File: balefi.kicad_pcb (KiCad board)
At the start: 2 copper layers, 2 parts, among them J1 Connectors_EFI_ECUs_Con_82521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, M2 Module:mega-mcu100/0.3

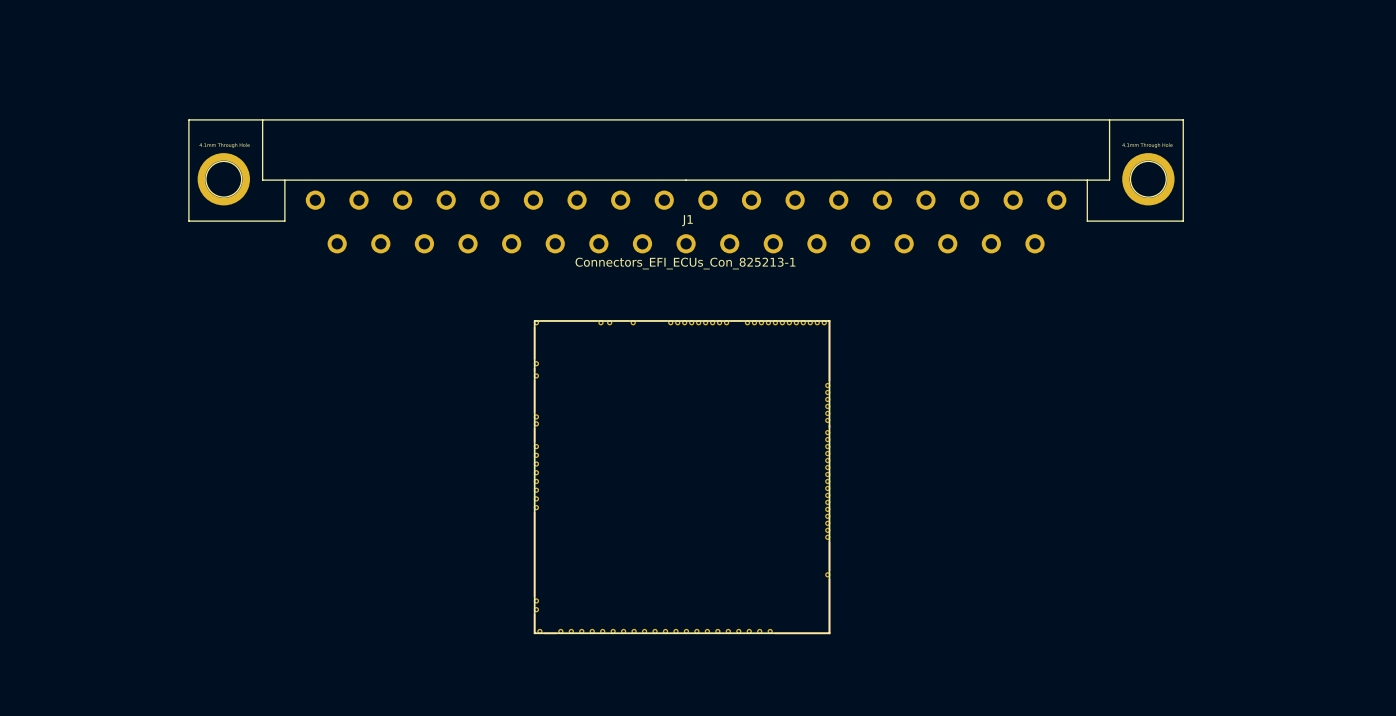
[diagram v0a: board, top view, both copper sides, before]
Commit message: Added outer dimmensions for PCB, added origin point
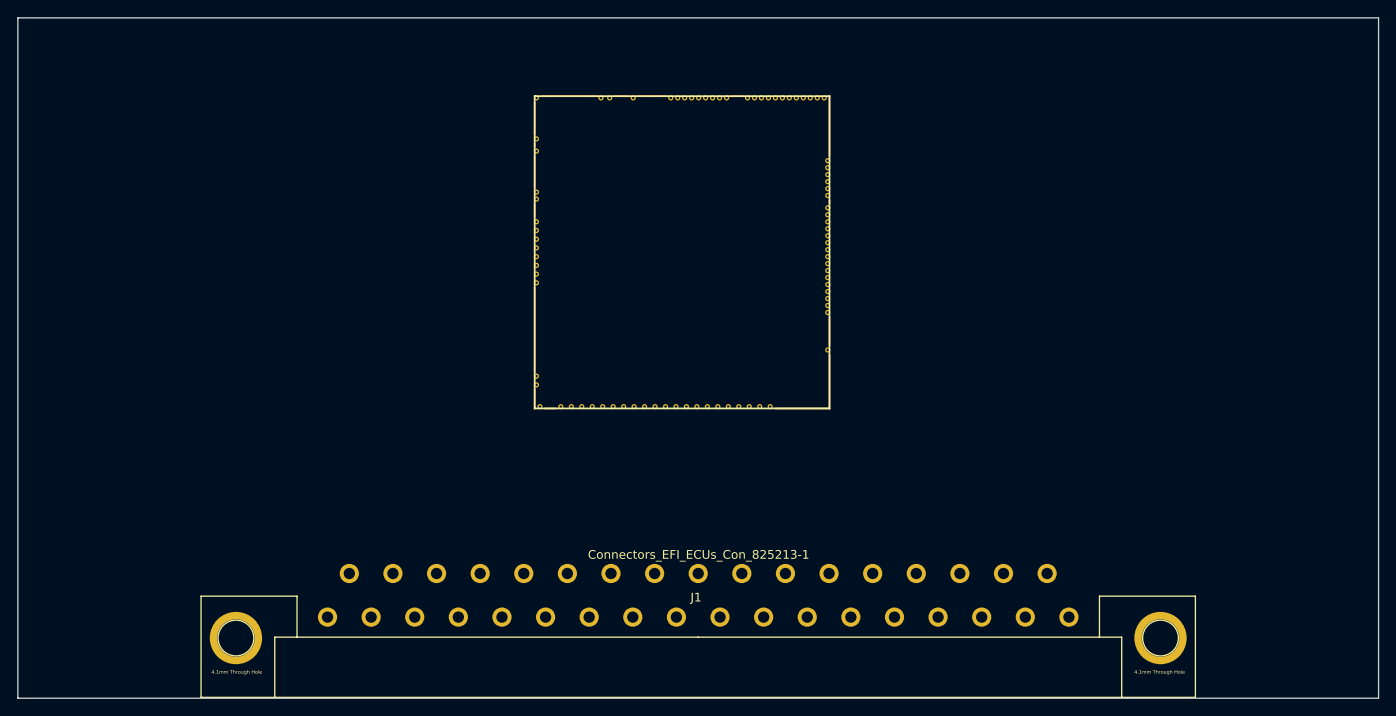
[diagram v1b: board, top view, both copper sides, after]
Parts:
- moved J1 52.4 mm to (150.0, 130.0), turned to 180 degrees
- moved M2 25.8 mm to (131.1, 103.9)
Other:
- board outline added: 156 x 78 mm

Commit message: Started designing schematic
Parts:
- added ?: , , F.Cu at (77.2, 63.4)
- added ?: , , F.Cu at (75.8, 130.0)
- added H1: MountingHole_Pad, MountingHole:MountingHole_3.7mm_Pad_Via, F.Cu at (87.8, 131.0)
- added H2: MountingHole_Pad, MountingHole:MountingHole_3.7mm_Pad_Via, F.Cu at (211.8, 131.0)
- added H3: MountingHole, MountingHole:MountingHole_3.7mm, F.Cu at (156.0, 63.0)
- J1: footprint rusefi_lib:825213-1 -> rusefi_lib:825213-1_FIAT
- moved M2 42.4 mm to (173.3, 99.2)
- moved J1 8.00 mm to (150.0, 138.0)
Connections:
- J1 pad 1: unconnected-(J1-Pad1) -> /IGN14
- J1 pad 10: unconnected-(J1-Pad10) -> /CANL
- J1 pad 11: unconnected-(J1-Pad11) -> /CRANK-
- J1 pad 12: unconnected-(J1-Pad12) -> /AGND
- J1 pad 13: unconnected-(J1-Pad13) -> /CLT
- J1 pad 14: unconnected-(J1-Pad14) -> /5V
- J1 pad 15: unconnected-(J1-Pad15) -> /CANH
- J1 pad 16: unconnected-(J1-Pad16) -> /AGND
- J1 pad 17: unconnected-(J1-Pad17) -> /PGND
- J1 pad 18: unconnected-(J1-Pad18) -> /INJ1
- J1 pad 19: unconnected-(J1-Pad19) -> /IGN23
- J1 pad 2: unconnected-(J1-Pad2) -> /ETB2
- J1 pad 20: unconnected-(J1-Pad20) -> /ETB1
- J1 pad 21: unconnected-(J1-Pad21) -> /INJ3
- J1 pad 22: unconnected-(J1-Pad22) -> /TACHO_OUT
- J1 pad 23: unconnected-(J1-Pad23) -> /FPUMP_RELAY
- J1 pad 24: unconnected-(J1-Pad24) -> /FUEL_PRESS
- J1 pad 25: unconnected-(J1-Pad25) -> /OIL_TEMP
- J1 pad 26: unconnected-(J1-Pad26) -> /IGNITION
- J1 pad 27: unconnected-(J1-Pad27) -> /PPS1_IN
- J1 pad 28: unconnected-(J1-Pad28) -> /CRANK+
- J1 pad 29: unconnected-(J1-Pad29) -> /KNOCK_IN
- J1 pad 3: unconnected-(J1-Pad3) -> /FAN_OUT
- J1 pad 30: unconnected-(J1-Pad30) -> /TPS
- J1 pad 31: unconnected-(J1-Pad31) -> /IAT
- J1 pad 32: unconnected-(J1-Pad32) -> /MAP
- J1 pad 33: unconnected-(J1-Pad33) -> /CAM
- J1 pad 34: unconnected-(J1-Pad34) -> /FLEX_IN
- J1 pad 35: unconnected-(J1-Pad35) -> /INJ2
- J1 pad 4: unconnected-(J1-Pad4) -> /INJ4
- J1 pad 5: unconnected-(J1-Pad5) -> /BOOST_OUT
- J1 pad 6: unconnected-(J1-Pad6) -> /MIL
- J1 pad 7: unconnected-(J1-Pad7) -> /VSS
- J1 pad 8: unconnected-(J1-Pad8) -> /OIL_PRESS
- J1 pad 9: unconnected-(J1-Pad9) -> /PPS2_IN
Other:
- board size 156 x 78 mm -> 146 x 78 mm

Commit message: a lot of changes
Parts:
- removed ? (x2): , 
- removed M2: Module:mega-mcu100/0.3, hellen-one-mega-mcu100-0.3:mega-mcu100
- added C1: 10nF, Capacitor_SMD:C_0402_1005Metric, F.Cu at (58.4, 75.1)
- added C10: 10nF, Capacitor_SMD:C_0402_1005Metric, F.Cu at (119.7, 117.3)
- added C100: 10uF, Capacitor_SMD:C_1206_3216Metric, F.Cu at (86.2, 73.0)
- added C101: 10uF, Capacitor_SMD:C_1206_3216Metric, F.Cu at (86.2, 76.4)
- added C102: 10uF, Capacitor_SMD:C_1206_3216Metric, F.Cu at (86.2, 79.7)
- added C103: 100nF, Capacitor_SMD:C_0402_1005Metric, F.Cu at (90.5, 83.5)
- added C104: 10uF, Capacitor_SMD:C_1206_3216Metric, F.Cu at (86.2, 83.1)
- added C105: 100nF, Capacitor_SMD:C_0402_1005Metric, F.Cu at (90.5, 85.5)
- added C106: 100nF, Capacitor_SMD:C_0402_1005Metric, F.Cu at (167.5, 65.0)
- added C107: 1uF, Capacitor_SMD:C_0805_2012Metric, F.Cu at (147.3, 116.0)
- added C108: 100nF, Capacitor_SMD:C_0402_1005Metric, F.Cu at (145.7, 116.8)
- added C109: 10nF, Capacitor_SMD:C_0402_1005Metric, F.Cu at (142.5, 117.8)
- added C11: 100uF, Capacitor_SMD:CP_Elec_8x10, F.Cu at (212.0, 87.7)
- added C12: 1uF, Capacitor_SMD:C_0805_2012Metric, F.Cu at (212.0, 77.2)
- added C13: 100nF, Capacitor_SMD:C_0402_1005Metric, F.Cu at (212.2, 75.6)
- added C14: 100nF, Capacitor_SMD:C_0402_1005Metric, F.Cu at (210.2, 74.0)
- added C15: 10uF, Capacitor_SMD:C_1206_3216Metric, F.Cu at (206.8, 74.4)
- added C16: 10uF, Capacitor_SMD:C_1206_3216Metric, F.Cu at (206.8, 76.8)
- added C17: 10uF, Capacitor_SMD:C_1206_3216Metric, F.Cu at (206.8, 79.2)
- added C18: 10uF, Capacitor_SMD:C_1206_3216Metric, F.Cu at (202.2, 79.2)
- added C19: 10uF, Capacitor_SMD:C_1206_3216Metric, F.Cu at (202.2, 76.8)
- added C2: 10nF, Capacitor_SMD:C_0402_1005Metric, F.Cu at (58.4, 77.6)
- added C20: 10uF, Capacitor_SMD:C_1206_3216Metric, F.Cu at (202.2, 74.4)
- added C21: 10uF, Capacitor_SMD:C_1206_3216Metric, F.Cu at (212.2, 118.0)
- added C22: 10uF, Capacitor_SMD:C_1206_3216Metric, F.Cu at (214.8, 93.3)
- added C23: 10nF, Capacitor_SMD:C_0402_1005Metric, F.Cu at (214.1, 66.5)
- added C24: 1uF, Capacitor_SMD:C_0805_2012Metric, F.Cu at (177.1, 111.2)
- added C25: 1uF, Capacitor_SMD:C_0805_2012Metric, F.Cu at (186.8, 110.9)
- added C26: 10uF, Capacitor_SMD:C_1206_3216Metric, F.Cu at (194.0, 93.5)
- added C27: 100nF, Capacitor_SMD:C_0402_1005Metric, F.Cu at (49.7, 96.8)
- added C28: 100nF, Capacitor_SMD:C_0402_1005Metric, F.Cu at (195.1, 95.3)
- added C29: 100nF, Capacitor_SMD:C_0402_1005Metric, F.Cu at (195.1, 100.7)
- added C3: 10nF, Capacitor_SMD:C_0402_1005Metric, F.Cu at (58.4, 80.1)
- added C30: 1uF, Capacitor_SMD:C_0805_2012Metric, F.Cu at (194.6, 102.3)
- added C31: 10uF, Capacitor_SMD:C_1206_3216Metric, F.Cu at (194.0, 104.7)
- added C32: 100nF, Capacitor_SMD:C_0402_1005Metric, F.Cu at (79.2, 26.8)
- added C33: 390pF, Capacitor_SMD:C_0402_1005Metric, F.Cu at (71.0, 17.0)
- added C34: 390pF, Capacitor_SMD:C_0402_1005Metric, F.Cu at (71.0, 19.5)
- added C35: 390pF, Capacitor_SMD:C_0402_1005Metric, F.Cu at (71.0, 22.0)
- added C36: 390pF, Capacitor_SMD:C_0402_1005Metric, F.Cu at (71.0, 24.5)
- added C37: 100nF, Capacitor_SMD:C_0402_1005Metric, F.Cu at (98.5, 27.0)
- added C38: 390pF, Capacitor_SMD:C_0402_1005Metric, F.Cu at (90.3, 17.2)
- added C39: 390pF, Capacitor_SMD:C_0402_1005Metric, F.Cu at (90.3, 19.7)
- added C4: 100nF, Capacitor_SMD:C_0402_1005Metric, F.Cu at (58.4, 82.6)
- added C40: 390pF, Capacitor_SMD:C_0402_1005Metric, F.Cu at (90.3, 22.2)
- added C41: 390pF, Capacitor_SMD:C_0402_1005Metric, F.Cu at (90.3, 24.8)
- added C42: 100nF, Capacitor_SMD:C_0402_1005Metric, F.Cu at (93.0, 101.1)
- added C43: 100nF, Capacitor_SMD:C_0402_1005Metric, F.Cu at (93.0, 99.0)
- added C44: 100nF, Capacitor_SMD:C_0402_1005Metric, F.Cu at (124.3, 89.0)
- added C45: 100nF, Capacitor_SMD:C_0402_1005Metric, F.Cu at (138.3, 91.3)
- added C46: 100nF, Capacitor_SMD:C_0402_1005Metric, F.Cu at (133.9, 71.9)
- added C47: 100nF, Capacitor_SMD:C_0402_1005Metric, F.Cu at (122.5, 76.8)
- added C48: 100nF, Capacitor_SMD:C_0402_1005Metric, F.Cu at (141.9, 76.3)
- added C49: 100nF, Capacitor_SMD:C_0402_1005Metric, F.Cu at (129.6, 72.0)
- added C5: 100nF, Capacitor_SMD:C_0402_1005Metric, F.Cu at (106.2, 114.3)
- added C50: 10uF, Capacitor_SMD:C_1206_3216Metric, F.Cu at (120.5, 80.7)
- added C51: 100nF, Capacitor_SMD:C_0402_1005Metric, F.Cu at (136.3, 72.0)
- added C52: 100nF, Capacitor_SMD:C_0402_1005Metric, F.Cu at (128.1, 71.9)
- added C53: 100nF, Capacitor_SMD:C_0402_1005Metric, F.Cu at (146.8, 84.1)
- added C54: 2.2uF, Capacitor_SMD:C_0805_2012Metric, F.Cu at (120.8, 87.5)
- added C55: 2.2uF, Capacitor_SMD:C_0805_2012Metric, F.Cu at (121.1, 83.9)
- added C56: 15pF, Capacitor_SMD:C_0402_1005Metric, F.Cu at (137.0, 67.6)
- added C57: 15pF, Capacitor_SMD:C_0402_1005Metric, F.Cu at (135.6, 67.6)
- added C58: 6pF, Capacitor_SMD:C_0402_1005Metric, F.Cu at (134.0, 67.2)
- added C59: 6pF, Capacitor_SMD:C_0402_1005Metric, F.Cu at (129.3, 67.3)
- added C6: 100uF, Capacitor_SMD:CP_Elec_8x10, F.Cu at (107.7, 106.3)
- added C60: 100nF, Capacitor_SMD:C_0402_1005Metric, F.Cu at (117.8, 26.7)
- added C61: 390pF, Capacitor_SMD:C_0402_1005Metric, F.Cu at (109.6, 16.9)
- added C62: 390pF, Capacitor_SMD:C_0402_1005Metric, F.Cu at (109.6, 19.4)
- added C63: 390pF, Capacitor_SMD:C_0402_1005Metric, F.Cu at (109.6, 22.0)
- added C64: 390pF, Capacitor_SMD:C_0402_1005Metric, F.Cu at (109.6, 24.5)
- added C65: 100nF, Capacitor_SMD:C_0402_1005Metric, F.Cu at (168.9, 101.4)
- added C66: 4.7nF, Capacitor_SMD:C_0402_1005Metric, F.Cu at (168.9, 114.7)
- added C67: 100nF, Capacitor_SMD:C_0402_1005Metric, F.Cu at (165.6, 107.8)
- added C68: 10nF, Capacitor_SMD:C_0402_1005Metric, F.Cu at (73.5, 35.4)
- added C69: 10nF, Capacitor_SMD:C_0402_1005Metric, F.Cu at (73.5, 38.0)
- added C7: 1uF, Capacitor_SMD:C_0805_2012Metric, F.Cu at (103.8, 114.2)
- added C70: 10nF, Capacitor_SMD:C_0402_1005Metric, F.Cu at (73.5, 40.5)
- added C71: 10nF, Capacitor_SMD:C_0402_1005Metric, F.Cu at (73.5, 43.0)
- added C72: 10nF, Capacitor_SMD:C_0402_1005Metric, F.Cu at (111.5, 34.3)
- added C73: 10nF, Capacitor_SMD:C_0402_1005Metric, F.Cu at (111.5, 36.8)
- added C74: 10nF, Capacitor_SMD:C_0402_1005Metric, F.Cu at (111.5, 39.3)
- added C75: 10nF, Capacitor_SMD:C_0402_1005Metric, F.Cu at (111.5, 41.8)
- added C76: 10nF, Capacitor_SMD:C_0402_1005Metric, F.Cu at (92.0, 35.4)
- added C77: 10nF, Capacitor_SMD:C_0402_1005Metric, F.Cu at (92.0, 37.9)
- added C78: 10nF, Capacitor_SMD:C_0402_1005Metric, F.Cu at (92.0, 40.5)
- added C79: 10nF, Capacitor_SMD:C_0402_1005Metric, F.Cu at (92.0, 43.0)
- added C8: 100nF, Capacitor_SMD:C_0402_1005Metric, F.Cu at (104.3, 115.8)
- added C80: 100nF, Capacitor_SMD:C_0402_1005Metric, F.Cu at (157.7, 113.3)
- added C81: 2.2uF, Capacitor_SMD:C_0805_2012Metric, F.Cu at (156.0, 119.3)
- added C82: 2.2uF, Capacitor_SMD:C_0805_2012Metric, F.Cu at (156.0, 117.2)
- added C83: 3.3nF, Capacitor_SMD:C_0402_1005Metric, F.Cu at (161.2, 122.4)
- added C84: 47pF, Capacitor_SMD:C_0402_1005Metric, F.Cu at (160.2, 112.9)
- added C85: 680pF, Capacitor_SMD:C_0402_1005Metric, F.Cu at (162.4, 116.2)
- added C86: 330pF, Capacitor_SMD:C_0402_1005Metric, F.Cu at (159.2, 112.9)
- added C87: 100nF, Capacitor_SMD:C_0402_1005Metric, F.Cu at (139.0, 174.9)
- added C88: 10uF, Capacitor_SMD:C_1206_3216Metric, F.Cu at (156.5, 177.5)
- added C89: 1nF, Capacitor_SMD:C_0805_2012Metric, F.Cu at (144.4, 178.1)
- added C9: 10nF, Capacitor_SMD:C_0402_1005Metric, F.Cu at (106.2, 117.3)
- added C90: 1nF, Capacitor_SMD:C_0805_2012Metric, F.Cu at (147.4, 178.1)
- added C91: 10uF, Capacitor_SMD:C_1206_3216Metric, F.Cu at (190.7, 68.8)
- added C92: 100nF, Capacitor_SMD:C_0402_1005Metric, F.Cu at (190.7, 71.8)
- added C93: 10uF, Capacitor_SMD:C_1206_3216Metric, F.Cu at (86.2, 63.0)
- added C94: 100nF, Capacitor_SMD:C_0402_1005Metric, F.Cu at (90.5, 75.6)
- added C95: 100nF, Capacitor_SMD:C_0402_1005Metric, F.Cu at (90.5, 77.6)
- added C96: 10uF, Capacitor_SMD:C_1206_3216Metric, F.Cu at (86.2, 66.3)
- added C97: 10uF, Capacitor_SMD:C_1206_3216Metric, F.Cu at (86.2, 69.7)
- added C98: 100nF, Capacitor_SMD:C_0402_1005Metric, F.Cu at (90.5, 79.6)
- added C99: 100nF, Capacitor_SMD:C_0402_1005Metric, F.Cu at (90.5, 81.5)
- added D1: NSVRB751V40T1G, Diode_SMD:D_SOD-323, F.Cu at (70.5, 75.3)
- added D10: V3P6HM3_A/H, Diode_SMD:Vishay_SMPA, F.Cu at (209.1, 69.9)
- added D11: LED, LED_SMD:LED_0603_1608Metric, F.Cu at (175.1, 111.0)
- added D12: 1N4148WS, Diode_SMD:D_SOD-323, F.Cu at (195.3, 90.7)
- added D13: 1N4148WS, Diode_SMD:D_SOD-323, F.Cu at (193.3, 90.7)
- added D14: 1N4148WS, Diode_SMD:D_SOD-323, F.Cu at (138.4, 72.2)
- added D15: LED, LED_SMD:LED_0603_1608Metric, F.Cu at (91.3, 103.8)
- added D16: LED, LED_SMD:LED_0603_1608Metric, F.Cu at (100.2, 103.6)
- added D17: LED, LED_SMD:LED_0603_1608Metric, F.Cu at (122.4, 63.8)
- added D18: LED, LED_SMD:LED_0603_1608Metric, F.Cu at (122.4, 66.3)
- added D19: LED, LED_SMD:LED_0603_1608Metric, F.Cu at (122.4, 68.9)
- added D2: NSVRB751V40T1G, Diode_SMD:D_SOD-323, F.Cu at (70.5, 78.2)
- added D20: LED, LED_SMD:LED_0603_1608Metric, F.Cu at (122.4, 71.5)
- added D21: SZNUP2105L, Package_TO_SOT_SMD:SOT-23, F.Cu at (168.8, 117.8)
- added D22: NUP4202W1T2G, Package_TO_SOT_SMD:SOT-363_SC-70-6, F.Cu at (77.6, 52.0)
- added D23: NUP4202W1T2G, Package_TO_SOT_SMD:SOT-363_SC-70-6, F.Cu at (115.7, 50.9)
- added D24: NUP4202W1T2G, Package_TO_SOT_SMD:SOT-363_SC-70-6, F.Cu at (96.1, 52.0)
- added D25: LED, LED_SMD:LED_0603_1608Metric, F.Cu at (134.2, 174.3)
- added D26: LED, LED_SMD:LED_0603_1608Metric, F.Cu at (136.8, 174.3)
- added D27: 1N4148WS, Diode_SMD:D_SOD-323, F.Cu at (147.0, 76.5)
- added D28: LED, LED_SMD:LED_0603_1608Metric, F.Cu at (103.1, 70.7)
- added D29: V3P6HM3_A/H, Diode_SMD:Vishay_SMPA, F.Cu at (97.5, 71.4)
- added D3: NSVRB751V40T1G, Diode_SMD:D_SOD-323, F.Cu at (70.5, 81.2)
- added D30: PRTR5V0U2X, Package_TO_SOT_SMD:SOT-143, F.Cu at (191.0, 25.0)
- added D31: SZNUP2105L, Package_TO_SOT_SMD:SOT-23, F.Cu at (142.5, 121.5)
- added D4: NSVRB751V40T1G, Diode_SMD:D_SOD-323, F.Cu at (70.5, 84.1)
- added D5: MMSZ4688-TP, Diode_SMD:D_SOD-123, F.Cu at (59.3, 93.0)
- added D6: MMSZ4688-TP, Diode_SMD:D_SOD-123, F.Cu at (59.3, 96.4)
- added D7: V3P6HM3_A/H, Diode_SMD:Vishay_SMPA, F.Cu at (207.2, 116.5)
- added D8: LED, LED_SMD:LED_0603_1608Metric, F.Cu at (214.3, 117.2)
- added D9: LED, LED_SMD:LED_0603_1608Metric, F.Cu at (192.3, 76.9)
- added F1: 350 mA, Fuse:Fuse_1206_3216Metric, F.Cu at (53.5, 75.5)
- added F2: 350 mA, Fuse:Fuse_1206_3216Metric, F.Cu at (53.5, 78.7)
- added F3: 350 mA, Fuse:Fuse_1206_3216Metric, F.Cu at (53.5, 82.0)
- added F4: 350 mA, Fuse:Fuse_1206_3216Metric, F.Cu at (53.5, 85.3)
- added F5: 350 mA, Fuse:Fuse_1206_3216Metric, F.Cu at (53.5, 88.6)
- added F6: 350 mA, Fuse:Fuse_1206_3216Metric, F.Cu at (102.8, 76.3)
- added F7: 350 mA, Fuse:Fuse_1206_3216Metric, F.Cu at (102.8, 79.6)
- added FB1: 600 ohm 500mA, Resistor_SMD:R_0603_1608Metric, F.Cu at (102.0, 82.5)
- added J2: Conn_01x06_Pin, Connector_PinHeader_2.54mm:PinHeader_1x06_P2.54mm_Vertical, F.Cu at (113.0, 98.1)
- added J3: Conn_01x03_Pin, Connector_PinHeader_2.54mm:PinHeader_1x03_P2.54mm_Vertical, F.Cu at (118.0, 98.0)
- added J4: MEM2067-02-180-00-A, footprints:MEM2067-02-180-00-A, F.Cu at (179.2, 69.2)
- added J5: Conn_01x06_Pin, Connector_JST:JST_PH_B6B-PH-K_1x06_P2.00mm_Vertical, F.Cu at (187.8, 18.9)
- added L1: 3,3uH, Inductor_SMD:L_TDK_VLS6045EX_VLS6045AF, F.Cu at (204.1, 69.9)
- added L2: 3,3uH, Inductor_SMD:L_TDK_VLS6045EX_VLS6045AF, F.Cu at (214.3, 98.3)
- added L3: BLM18SP102SN1D, Inductor_SMD:L_0603_1608Metric_Pad1.05x0.95mm_HandSolder, F.Cu at (145.1, 121.7)
- added L4: BLM18SP102SN1D, Inductor_SMD:L_0603_1608Metric_Pad1.05x0.95mm_HandSolder, F.Cu at (139.9, 121.7)
- added NT1: NetTie_2, NetTie:NetTie-2_SMD_Pad2.0mm, F.Cu at (185.0, 119.0)
- added Q1: VND14NV04TR-E, Package_TO_SOT_SMD:TO-252-2, F.Cu at (33.9, 173.7)
- added Q10: PJA3460, Package_TO_SOT_SMD:SOT-23-3, F.Cu at (48.2, 89.4)
- added Q11: PJA3460, Package_TO_SOT_SMD:SOT-23-3, F.Cu at (48.2, 93.8)
- added Q12: DMG2307LQ-7, Package_TO_SOT_SMD:SOT-23-3, F.Cu at (94.5, 76.9)
- added Q13: RUC002N05HZGT116, Package_TO_SOT_SMD:SOT-23, F.Cu at (91.5, 63.5)
- added Q14: DMG2307LQ-7, Package_TO_SOT_SMD:SOT-23-3, F.Cu at (94.5, 81.3)
- added Q15: RUC002N05HZGT116, Package_TO_SOT_SMD:SOT-23, F.Cu at (91.5, 68.0)
- added Q2: VND14NV04TR-E, Package_TO_SOT_SMD:TO-252-2, F.Cu at (62.5, 174.0)
- added Q3: VND14NV04TR-E, Package_TO_SOT_SMD:TO-252-2, F.Cu at (49.4, 174.2)
- added Q4: VND14NV04TR-E, Package_TO_SOT_SMD:TO-252-2, F.Cu at (33.7, 157.5)
- added Q5: RGPR30BM40HRTL, Package_TO_SOT_SMD:TO-252-2, F.Cu at (86.8, 110.0)
- added Q6: RGPR30BM40HRTL, Package_TO_SOT_SMD:TO-252-2, F.Cu at (95.8, 110.0)
- added Q7: PJA3460, Package_TO_SOT_SMD:SOT-23-3, F.Cu at (48.2, 76.0)
- added Q8: PJA3460, Package_TO_SOT_SMD:SOT-23-3, F.Cu at (48.2, 80.5)
- added Q9: PJA3460, Package_TO_SOT_SMD:SOT-23-3, F.Cu at (48.2, 84.9)
- added R1: 330, Resistor_SMD:R_0402_1005Metric, F.Cu at (29.0, 179.0)
- added R10: 1k, Resistor_SMD:R_0402_1005Metric, F.Cu at (98.0, 102.3)
- added R100: 680k, Resistor_SMD:R_0402_1005Metric, F.Cu at (115.0, 42.0)
- added R101: 680k, Resistor_SMD:R_0402_1005Metric, F.Cu at (115.0, 44.0)
- added R102: 680k, Resistor_SMD:R_0402_1005Metric, F.Cu at (115.0, 46.0)
- added R103: 680k, Resistor_SMD:R_0402_1005Metric, F.Cu at (115.0, 48.0)
- added R104: 680k, Resistor_SMD:R_0402_1005Metric, F.Cu at (95.5, 35.2)
- added R105: 680k, Resistor_SMD:R_0402_1005Metric, F.Cu at (95.5, 37.2)
- added R106: 680k, Resistor_SMD:R_0402_1005Metric, F.Cu at (95.5, 39.1)
- added R107: 680k, Resistor_SMD:R_0402_1005Metric, F.Cu at (95.5, 41.1)
- added R108: 4k7, Resistor_SMD:R_0402_1005Metric, F.Cu at (92.0, 45.5)
- added R109: 4k7, Resistor_SMD:R_0402_1005Metric, F.Cu at (92.0, 48.0)
- added R11: 10k, Resistor_SMD:R_1206_3216Metric, F.Cu at (53.5, 91.9)
- added R110: 4k7, Resistor_SMD:R_0402_1005Metric, F.Cu at (92.0, 50.5)
- added R111: 4k7, Resistor_SMD:R_0402_1005Metric, F.Cu at (92.0, 53.0)
- added R112: 680k, Resistor_SMD:R_0402_1005Metric, F.Cu at (95.5, 43.1)
- added R113: 680k, Resistor_SMD:R_0402_1005Metric, F.Cu at (95.5, 45.1)
- added R114: 680k, Resistor_SMD:R_0402_1005Metric, F.Cu at (95.5, 47.1)
- added R115: 680k, Resistor_SMD:R_0402_1005Metric, F.Cu at (95.5, 49.1)
- added R116: 330, Resistor_SMD:R_0402_1005Metric, F.Cu at (157.2, 115.2)
- added R117: 330, Resistor_SMD:R_0402_1005Metric, F.Cu at (156.1, 115.2)
- added R118: 12k, Resistor_SMD:R_0402_1005Metric, F.Cu at (161.9, 117.8)
- added R119: 100k, Resistor_SMD:R_0402_1005Metric, F.Cu at (162.2, 114.6)
- added R12: 330, Resistor_SMD:R_0402_1005Metric, F.Cu at (58.4, 85.1)
- added R120: 33k, Resistor_SMD:R_0402_1005Metric, F.Cu at (161.7, 113.0)
- added R121: 100k, Resistor_SMD:R_0402_1005Metric, F.Cu at (160.2, 121.4)
- added R122: 470k, Resistor_SMD:R_0402_1005Metric, F.Cu at (158.7, 121.0)
- added R123: 10k, Resistor_SMD:R_1206_3216Metric, F.Cu at (110.6, 181.6)
- added R124: 10k, Resistor_SMD:R_1206_3216Metric, F.Cu at (113.8, 181.6)
- added R125: 10k, Resistor_SMD:R_1206_3216Metric, F.Cu at (126.0, 166.8)
- added R126: 10k, Resistor_SMD:R_1206_3216Metric, F.Cu at (126.0, 169.2)
- added R127: 10k, Resistor_SMD:R_0402_1005Metric, F.Cu at (134.1, 178.3)
- added R128: 10k, Resistor_SMD:R_0402_1005Metric, F.Cu at (136.6, 178.3)
- added R129: 10k, Resistor_SMD:R_0402_1005Metric, F.Cu at (139.1, 178.3)
- added R13: 330, Resistor_SMD:R_0402_1005Metric, F.Cu at (58.4, 87.6)
- added R130: 10k, Resistor_SMD:R_0402_1005Metric, F.Cu at (141.7, 178.3)
- added R131: 5k1, Resistor_SMD:R_0603_1608Metric, F.Cu at (150.4, 178.1)
- added R132: 10k, Resistor_SMD:R_1206_3216Metric, F.Cu at (141.0, 183.1)
- added R133: 10k, Resistor_SMD:R_1206_3216Metric, F.Cu at (144.3, 183.1)
- added R134: 10k, Resistor_SMD:R_1206_3216Metric, F.Cu at (147.6, 183.1)
- added R135: 10k, Resistor_SMD:R_1206_3216Metric, F.Cu at (150.8, 183.1)
- added R136: 5k1, Resistor_SMD:R_0603_1608Metric, F.Cu at (153.3, 178.1)
- added R137: 10k, Resistor_SMD:R_1206_3216Metric, F.Cu at (154.1, 183.1)
- added R138: 10k, Resistor_SMD:R_1206_3216Metric, F.Cu at (157.4, 183.1)
- added R139: 4k7, Resistor_SMD:R_0402_1005Metric, F.Cu at (146.8, 79.2)
- added R14: 330, Resistor_SMD:R_0402_1005Metric, F.Cu at (58.4, 90.1)
- added R140: 10k, Resistor_SMD:R_0402_1005Metric, F.Cu at (190.5, 73.7)
- added R141: 1R, Resistor_SMD:R_0603_1608Metric, F.Cu at (192.9, 69.3)
- added R142: 10k, Resistor_SMD:R_0402_1005Metric, F.Cu at (102.0, 85.0)
- added R143: 10k, Resistor_SMD:R_0402_1005Metric, F.Cu at (98.5, 75.7)
- added R144: 10k, Resistor_SMD:R_0402_1005Metric, F.Cu at (98.5, 77.6)
- added R145: 10k, Resistor_SMD:R_0402_1005Metric, F.Cu at (98.5, 79.6)
- added R146: 10k, Resistor_SMD:R_0402_1005Metric, F.Cu at (98.5, 81.6)
- added R147: 5k1, Resistor_SMD:R_0603_1608Metric, F.Cu at (186.9, 24.0)
- added R148: 5k1, Resistor_SMD:R_0603_1608Metric, F.Cu at (186.9, 26.5)
- added R149: 22, Resistor_SMD:R_0402_1005Metric, F.Cu at (143.2, 80.5)
- added R15: 330, Resistor_SMD:R_0402_1005Metric, F.Cu at (62.4, 75.1)
- added R150: 22, Resistor_SMD:R_0402_1005Metric, F.Cu at (143.2, 81.9)
- added R151: 22, Resistor_SMD:R_0402_1005Metric, F.Cu at (143.2, 79.5)
- added R152: 22, Resistor_SMD:R_0402_1005Metric, F.Cu at (171.8, 66.5)
- added R153: 22, Resistor_SMD:R_0402_1005Metric, F.Cu at (141.8, 108.5)
- added R154: 22, Resistor_SMD:R_0402_1005Metric, F.Cu at (142.8, 88.3)
- added R155: 22, Resistor_SMD:R_0402_1005Metric, F.Cu at (142.9, 91.5)
- added R16: 68k, Resistor_SMD:R_0402_1005Metric, F.Cu at (62.4, 77.6)
- added R17: 68k, Resistor_SMD:R_0402_1005Metric, F.Cu at (62.4, 80.1)
- added R18: 68k, Resistor_SMD:R_0402_1005Metric, F.Cu at (62.4, 82.6)
- added R19: 68k, Resistor_SMD:R_0402_1005Metric, F.Cu at (62.4, 85.1)
- added R2: 68k, Resistor_SMD:R_0402_1005Metric, F.Cu at (29.0, 181.5)
- added R20: 33k, Resistor_SMD:R_0402_1005Metric, F.Cu at (62.4, 87.6)
- added R21: 33k, Resistor_SMD:R_0402_1005Metric, F.Cu at (62.4, 90.1)
- added R22: 33k, Resistor_SMD:R_0402_1005Metric, F.Cu at (66.4, 75.1)
- added R23: 330, Resistor_SMD:R_0402_1005Metric, F.Cu at (66.4, 77.6)
- added R24: 100k, Resistor_SMD:R_0402_1005Metric, F.Cu at (66.4, 80.1)
- added R25: 68k, Resistor_SMD:R_0402_1005Metric, F.Cu at (66.4, 82.6)
- added R26: 4k7, Resistor_SMD:R_0402_1005Metric, F.Cu at (121.8, 113.3)
- added R27: 33k, Resistor_SMD:R_0402_1005Metric, F.Cu at (214.6, 119.8)
- added R28: 68k, Resistor_SMD:R_0402_1005Metric, F.Cu at (206.2, 81.0)
- added R29: 10k, Resistor_SMD:R_0402_1005Metric, F.Cu at (216.6, 72.8)
- added R3: 330, Resistor_SMD:R_0402_1005Metric, F.Cu at (57.6, 179.3)
- added R30: 10k, Resistor_SMD:R_0402_1005Metric, F.Cu at (192.4, 79.5)
- added R31: 12k, Resistor_SMD:R_0402_1005Metric, F.Cu at (208.2, 81.0)
- added R32: 1R, Resistor_SMD:R_0603_1608Metric, F.Cu at (211.8, 121.2)
- added R33: 10k, Resistor_SMD:R_0402_1005Metric, F.Cu at (174.8, 113.2)
- added R34: 10k, Resistor_SMD:R_0402_1005Metric, F.Cu at (181.9, 115.2)
- added R35: 1k, Resistor_SMD:R_0402_1005Metric, F.Cu at (46.8, 97.0)
- added R36: 2k7, Resistor_SMD:R_0402_1005Metric, F.Cu at (75.0, 17.0)
- added R37: 2k7, Resistor_SMD:R_0402_1005Metric, F.Cu at (75.0, 19.5)
- added R38: 2k7, Resistor_SMD:R_0402_1005Metric, F.Cu at (75.0, 22.0)
- added R39: 2k7, Resistor_SMD:R_0402_1005Metric, F.Cu at (75.0, 24.5)
- added R4: 68k, Resistor_SMD:R_0402_1005Metric, F.Cu at (57.6, 181.8)
- added R40: 2k7, Resistor_SMD:R_0402_1005Metric, F.Cu at (79.0, 17.0)
- added R41: 2k7, Resistor_SMD:R_0402_1005Metric, F.Cu at (79.0, 19.5)
- added R42: 2k7, Resistor_SMD:R_0402_1005Metric, F.Cu at (79.0, 22.0)
- added R43: 2k7, Resistor_SMD:R_0402_1005Metric, F.Cu at (79.0, 24.5)
- added R44: 2k7, Resistor_SMD:R_0402_1005Metric, F.Cu at (94.3, 17.2)
- added R45: 2k7, Resistor_SMD:R_0402_1005Metric, F.Cu at (94.3, 19.7)
- added R46: 2k7, Resistor_SMD:R_0402_1005Metric, F.Cu at (94.3, 22.2)
- added R47: 2k7, Resistor_SMD:R_0402_1005Metric, F.Cu at (94.3, 24.8)
- added R48: 2k7, Resistor_SMD:R_0402_1005Metric, F.Cu at (98.3, 17.2)
- added R49: 2k7, Resistor_SMD:R_0402_1005Metric, F.Cu at (98.3, 19.7)
- added R5: 330, Resistor_SMD:R_0402_1005Metric, F.Cu at (44.5, 179.5)
- added R50: 2k7, Resistor_SMD:R_0402_1005Metric, F.Cu at (98.3, 22.2)
- added R51: 2k7, Resistor_SMD:R_0402_1005Metric, F.Cu at (98.3, 24.8)
- added R52: 10, Resistor_SMD:R_0402_1005Metric, F.Cu at (93.8, 102.9)
- added R53: 10, Resistor_SMD:R_0402_1005Metric, F.Cu at (95.8, 102.9)
- added R54: 10k, Resistor_SMD:R_0402_1005Metric, F.Cu at (96.0, 96.7)
- added R55: 10k, Resistor_SMD:R_0402_1005Metric, F.Cu at (93.9, 96.7)
- added R56: 1k, Resistor_SMD:R_0402_1005Metric, F.Cu at (91.2, 106.3)
- added R57: 1k, Resistor_SMD:R_0402_1005Metric, F.Cu at (100.2, 106.2)
- added R58: 10k, Resistor_SMD:R_0402_1005Metric, F.Cu at (121.8, 99.4)
- added R59: 10k, Resistor_SMD:R_0402_1005Metric, F.Cu at (121.8, 97.4)
- added R6: 68k, Resistor_SMD:R_0402_1005Metric, F.Cu at (44.5, 182.0)
- added R60: 100, Resistor_SMD:R_0402_1005Metric, F.Cu at (121.8, 95.4)
- added R61: 10, Resistor_SMD:R_0402_1005Metric, F.Cu at (121.8, 93.4)
- added R62: 10, Resistor_SMD:R_0402_1005Metric, F.Cu at (121.8, 91.4)
- added R63: 1k, Resistor_SMD:R_0402_1005Metric, F.Cu at (126.4, 63.7)
- added R64: 0R, Resistor_SMD:R_0402_1005Metric, F.Cu at (121.8, 89.4)
- added R65: 1k, Resistor_SMD:R_0402_1005Metric, F.Cu at (126.4, 66.2)
- added R66: 1k, Resistor_SMD:R_0402_1005Metric, F.Cu at (126.4, 68.7)
- added R67: 1k, Resistor_SMD:R_0402_1005Metric, F.Cu at (126.4, 71.2)
- added R68: 2k7, Resistor_SMD:R_0402_1005Metric, F.Cu at (113.6, 16.9)
- added R69: 2k7, Resistor_SMD:R_0402_1005Metric, F.Cu at (113.6, 19.4)
- added R7: 330, Resistor_SMD:R_0402_1005Metric, F.Cu at (28.8, 162.8)
- added R70: 2k7, Resistor_SMD:R_0402_1005Metric, F.Cu at (113.6, 22.0)
- added R71: 2k7, Resistor_SMD:R_0402_1005Metric, F.Cu at (113.6, 24.5)
- added R72: 2k7, Resistor_SMD:R_0402_1005Metric, F.Cu at (117.7, 16.9)
- added R73: 2k7, Resistor_SMD:R_0402_1005Metric, F.Cu at (117.7, 19.4)
- added R74: 2k7, Resistor_SMD:R_0402_1005Metric, F.Cu at (117.7, 22.0)
- added R75: 2k7, Resistor_SMD:R_0402_1005Metric, F.Cu at (117.7, 24.5)
- added R76: 10, Resistor_SMD:R_0402_1005Metric, F.Cu at (169.5, 110.5)
- added R77: 60.4, Resistor_SMD:R_0805_2012Metric, F.Cu at (170.7, 112.7)
- added R78: 60.4, Resistor_SMD:R_0805_2012Metric, F.Cu at (167.1, 112.7)
- added R79: 10, Resistor_SMD:R_0402_1005Metric, F.Cu at (168.3, 110.5)
- added R8: 68k, Resistor_SMD:R_0402_1005Metric, F.Cu at (28.8, 165.3)
- added R80: 680k, Resistor_SMD:R_0402_1005Metric, F.Cu at (77.0, 35.2)
- added R81: 680k, Resistor_SMD:R_0402_1005Metric, F.Cu at (77.0, 37.2)
- added R82: 680k, Resistor_SMD:R_0402_1005Metric, F.Cu at (77.0, 39.2)
- added R83: 680k, Resistor_SMD:R_0402_1005Metric, F.Cu at (77.0, 41.1)
- added R84: 4k7, Resistor_SMD:R_0402_1005Metric, F.Cu at (73.5, 45.5)
- added R85: 4k7, Resistor_SMD:R_0402_1005Metric, F.Cu at (73.5, 48.0)
- added R86: 4k7, Resistor_SMD:R_0402_1005Metric, F.Cu at (73.5, 50.5)
- added R87: 4k7, Resistor_SMD:R_0402_1005Metric, F.Cu at (73.5, 53.0)
- added R88: 680k, Resistor_SMD:R_0402_1005Metric, F.Cu at (77.0, 43.1)
- added R89: 680k, Resistor_SMD:R_0402_1005Metric, F.Cu at (77.0, 45.1)
- added R9: 1k, Resistor_SMD:R_0402_1005Metric, F.Cu at (89.4, 103.0)
- added R90: 680k, Resistor_SMD:R_0402_1005Metric, F.Cu at (77.0, 47.1)
- added R91: 680k, Resistor_SMD:R_0402_1005Metric, F.Cu at (77.0, 49.1)
- added R92: 680k, Resistor_SMD:R_0402_1005Metric, F.Cu at (115.0, 34.0)
- added R93: 680k, Resistor_SMD:R_0402_1005Metric, F.Cu at (115.0, 36.0)
- added R94: 680k, Resistor_SMD:R_0402_1005Metric, F.Cu at (115.0, 38.0)
- added R95: 680k, Resistor_SMD:R_0402_1005Metric, F.Cu at (115.0, 40.0)
- added R96: 4k7, Resistor_SMD:R_0402_1005Metric, F.Cu at (111.5, 44.3)
- added R97: 4k7, Resistor_SMD:R_0402_1005Metric, F.Cu at (111.5, 46.9)
- added R98: 4k7, Resistor_SMD:R_0402_1005Metric, F.Cu at (111.5, 49.4)
- added R99: 4k7, Resistor_SMD:R_0402_1005Metric, F.Cu at (111.5, 51.9)
- added U1: TLE9201SG, footprints:Infineon_PG-DSO-12-17_ThermalVias, F.Cu at (113.0, 115.3)
- added U10: TJA1051T/3/2Z, Package_SO:SOIC-8_3.9x4.9mm_P1.27mm, F.Cu at (168.9, 105.8)
- added U11: MCP6282T-E/MS, Package_SO:MSOP-8_3x3mm_P0.65mm, F.Cu at (159.6, 117.2)
- added U12: MAX9926, Package_SO:QSOP-16_3.9x4.9mm_P0.635mm, F.Cu at (129.5, 176.1)
- added U13: REF3033, Package_TO_SOT_SMD:SOT-23, F.Cu at (91.5, 72.4)
- added U14: NCV1117DT33T5G, Package_TO_SOT_SMD:TO-252-2, F.Cu at (100.9, 65.3)
- added U15: LPS25HB, Package_LGA:ST_HLGA-10_2.5x2.5mm_P0.6mm_LayoutBorder3x2y, F.Cu at (168.1, 62.0)
- added U16: MAX31855KASA, Package_SO:SOIC-8_3.9x4.9mm_P1.27mm, F.Cu at (142.4, 113.2)
- added U2: LMR14020-Q1, Package_SO:Texas_R-PDSO-G8_EP2.95x4.9mm_Mask2.4x3.1mm_ThermalVias, F.Cu at (213.4, 71.2)
- added U3: TLS115, Package_SO:Texas_R-PDSO-G8_EP2.95x4.9mm_Mask2.4x3.1mm_ThermalVias, F.Cu at (181.9, 111.9)
- added U4: TPS7B6933QDBVRQ1, Package_TO_SOT_SMD:SOT-23-5, F.Cu at (194.6, 98.0)
- added U5: TLV9064, Package_SO:TSSOP-14_4.4x5mm_P0.65mm, F.Cu at (73.3, 29.1)
- added U6: TLV9064, Package_SO:TSSOP-14_4.4x5mm_P0.65mm, F.Cu at (92.7, 29.3)
- added U7: 74LVC2T45DC, Package_SO:VSSOP-8_2.3x2mm_P0.5mm, F.Cu at (94.8, 100.0)
- added U8: STM32F429VGTx, Package_QFP:LQFP-100_14x14mm_P0.5mm, F.Cu at (132.6, 82.0)
- added U9: TLV9064, Package_SO:TSSOP-14_4.4x5mm_P0.65mm, F.Cu at (112.0, 29.0)
- added Y1: 32.768kHz, Crystal:Crystal_SMD_2012-2Pin_2.0x1.2mm, F.Cu at (136.3, 69.7)
- added Y2: 20MHz, Crystal:Crystal_SMD_2520-4Pin_2.5x2.0mm, F.Cu at (131.7, 68.8)
- H1: value MountingHole_Pad -> MountingHole; footprint MountingHole:MountingHole_3.7mm_Pad_Via -> MountingHole:MountingHole_3.7mm
- H3: value MountingHole -> MountingHole_Pad; footprint MountingHole:MountingHole_3.7mm -> MountingHole:MountingHole_3.7mm_Pad_Via
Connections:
- net /AGND renamed GNDA
- H2 pad 1: unconnected-(H2-Pad1) -> GND
- J1 pad 14: /5V -> /5VP
- J1 pad 17: /PGND -> GND
- J1 pad 24: /FUEL_PRESS -> /INJ2
- J1 pad 25: /OIL_TEMP -> /EGT-
- J1 pad 26: /IGNITION -> /EGT+
- J1 pad 30: /TPS -> /TPS1
- J1 pad 33: /CAM -> /CAM-/HALL
- J1 pad 34: /FLEX_IN -> /CAM+
- J1 pad 35: /INJ2 -> /12V_RAW
- J1 pad 4: /INJ4 -> /MAIN_RELAY
- J1 pad 5: /BOOST_OUT -> /TPS2
- J1 pad 8: /OIL_PRESS -> /INJ4
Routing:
- net /VBAT: track 0.00 -> 3.31 mm
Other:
- board size 146 x 78 mm -> 136 x 78 mm
- copper layers 2 -> 4
- rule pad_to_mask_clearance: 0 -> 0.038
